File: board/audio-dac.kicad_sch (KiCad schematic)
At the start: 14 parts, among them J6 STEREO_OUT, U17 74HC373, U18 LM358

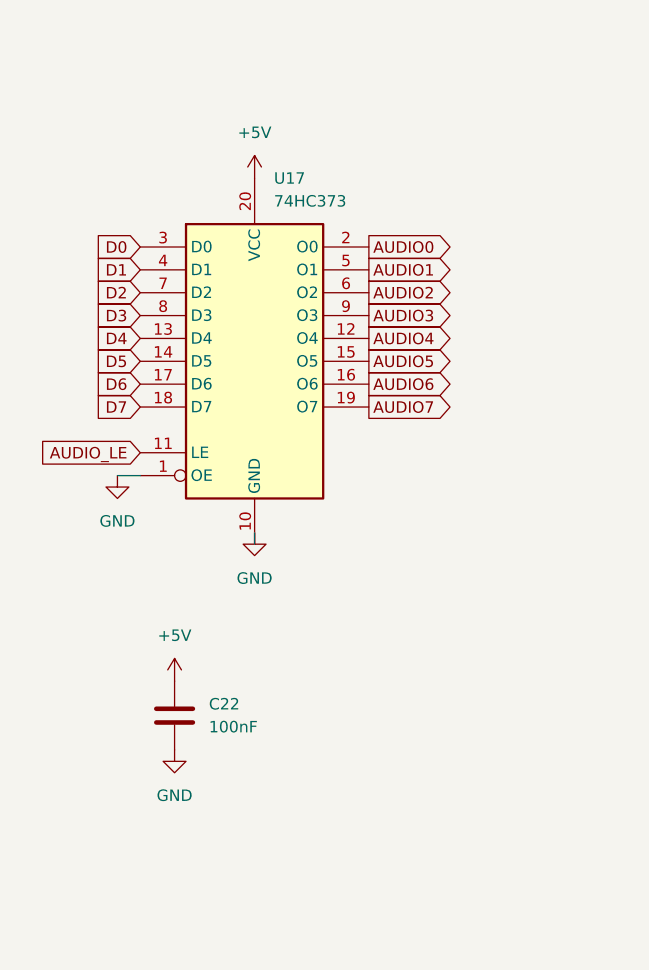
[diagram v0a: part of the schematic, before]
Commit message: add debug header
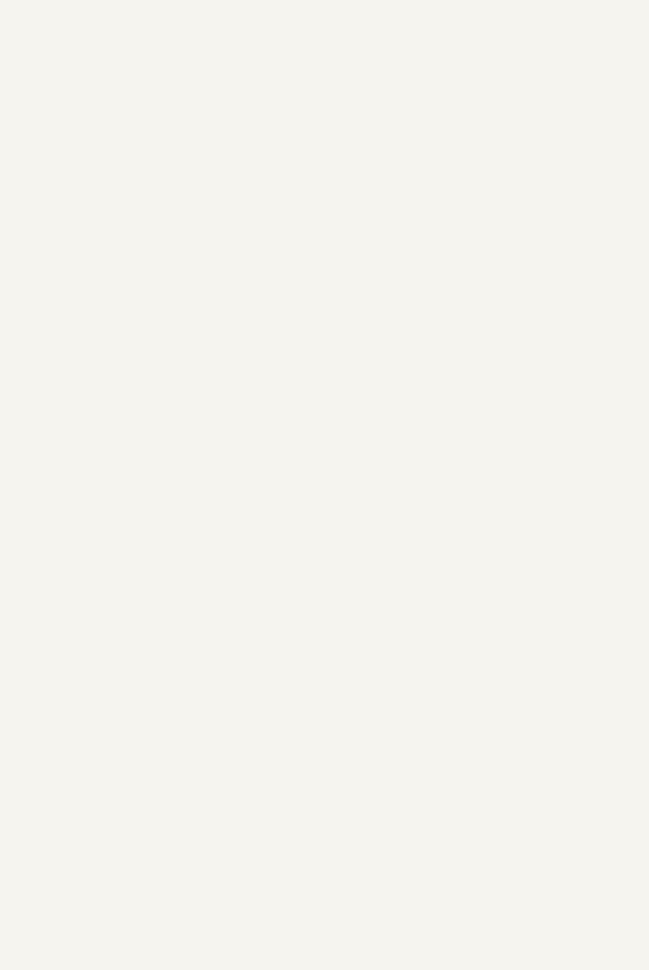
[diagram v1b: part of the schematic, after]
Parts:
- removed C22: 100nF, Capacitor_THT:C_Disc_D5.0mm_W2.5mm_P5.00mm, symbol Device:C
- removed U17: 74HC373, Package_DIP:DIP-20_W7.62mm, symbol 74xx:74HC373
